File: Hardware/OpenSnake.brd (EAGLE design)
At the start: 25.4 x 69.8 mm, 53 parts, among them Q1 16MHZ, U1 ATMEGA328P_TQFP, U2 317

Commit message: Adjusted tValues for better assembly sheet, created assembly sheet PDF
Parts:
- U1: value ATMEGA328P_TQFP -> ATMEGA328P

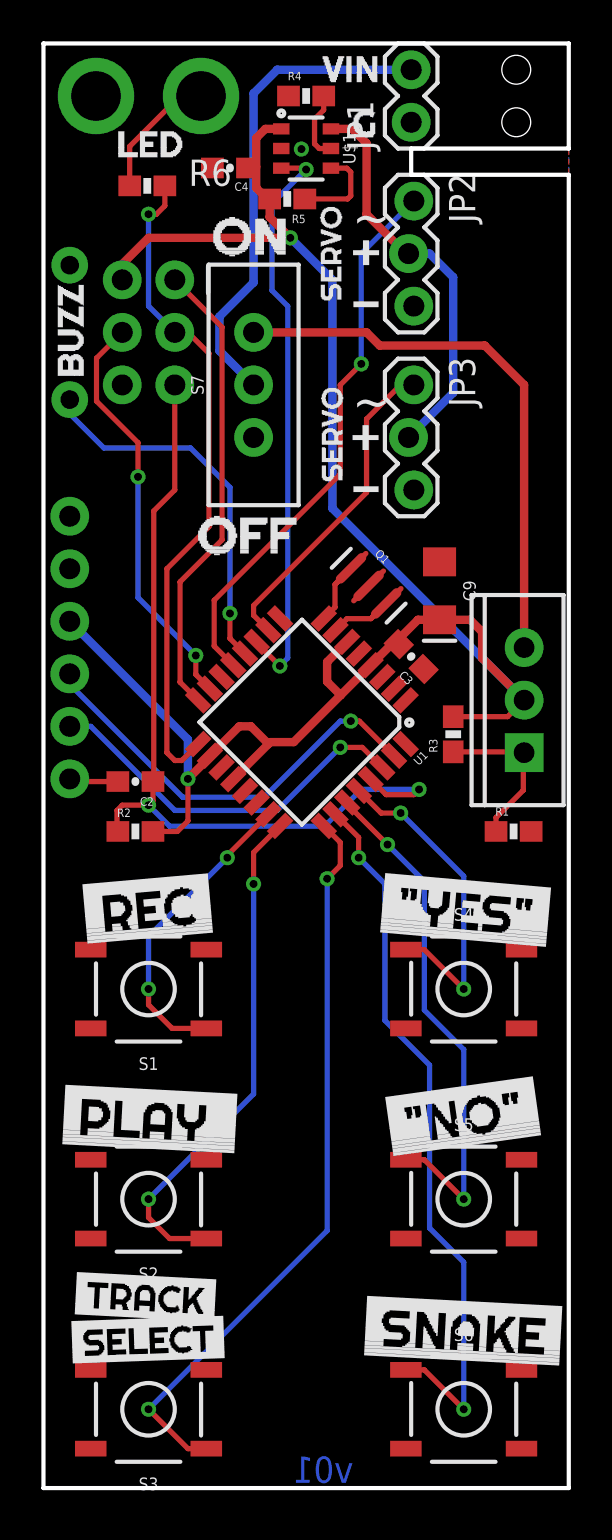
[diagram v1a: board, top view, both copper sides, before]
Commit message: Corrected RX/TX to 6-pin Serial programming header
I had these swapped on the header. Classic rookie mistake :)

-Swapped RX/TX on the serial header
-bumped version to v10 in sch and brd copper
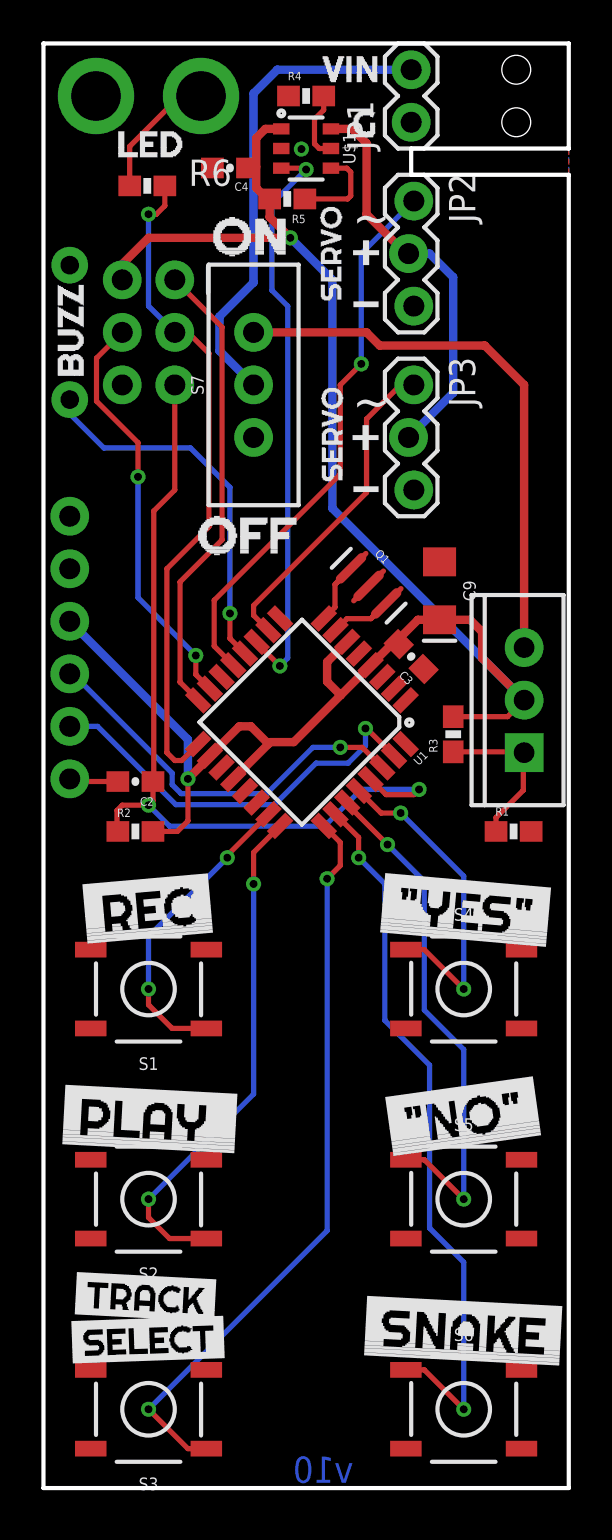
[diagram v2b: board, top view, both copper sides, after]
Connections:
- net RX: now also J1.P$3; no longer J1.P$2
- net TX: now also J1.P$2; no longer J1.P$3
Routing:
- net TX: track 20.7 -> 19.8 mm
- net RX: track 18.5 -> 19.2 mm
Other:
- board text added: "v10"
- board text removed: "v01"
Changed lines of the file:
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@@
 <wire x1="31.75" y1="52.07" x2="30.48" y2="53.34" width="0.2032" layer="49"/>
 <wire x1="31.75" y1="52.07" x2="30.48" y2="50.8" width="0.2032" layer="49"/>
-<text x="14.986" y="0.254" size="1.27" layer="16" font="vector" ratio="18" rot="MR0">v01</text>
+<text x="14.986" y="0.254" size="1.27" layer="16" font="vector" ratio="18" rot="MR0">v10</text>
 <rectangle x1="14.986" y1="57.0992" x2="16.2052" y2="57.3786" layer="21"/>
 <rectangle x1="14.986" y1="48.1584" x2="16.2052" y2="48.4378" layer="21"/>
@@
 <contactref element="U$1" pad="2"/>
 <contactref element="R4" pad="1"/>
-<contactref element="J1" pad="P$6"/>
-<contactref element="J1" pad="P$5"/>
 <polygon width="0.2032" layer="1">
 <vertex x="0" y="0"/>
@@
 <contactref element="LS1" pad="-"/>
 <via x="12.4714" y="64.7446" extent="1-16" drill="0.381"/>
+<contactref element="J1" pad="P$6"/>
+<contactref element="J1" pad="P$5"/>
 </signal>
 <signal name="SCK">
@@
 <wire x1="5.08" y1="57.15" x2="5.08" y2="61.595" width="0.254" layer="16"/>
 <via x="5.08" y="61.595" extent="1-16" drill="0.381"/>
-<wire x1="5.08" y1="61.595" x2="5.0520625" y2="61.6229375" width="0.254" layer="1"/>
 <wire x1="5.869040625" y1="62.003040625" x2="5.461" y2="61.595" width="0.254" layer="1"/>
 <wire x1="5.08" y1="61.595" x2="5.461" y2="61.595" width="0.254" layer="1"/>
@@
 <signal name="RX">
 <contactref element="U1" pad="30"/>
-<contactref element="J1" pad="P$2"/>
 <wire x1="16.382459375" y1="34.84459375" x2="15.413053125" y2="35.814" width="0.254" layer="1"/>
 <wire x1="15.413053125" y1="35.814" x2="14.351" y2="35.814" width="0.254" layer="1"/>
 <via x="14.351" y="35.814" extent="1-16" drill="0.381"/>
-<wire x1="14.351" y1="35.814" x2="11.303" y2="32.766" width="0.254" layer="16"/>
-<wire x1="2.286" y1="36.83" x2="1.27" y2="36.83" width="0.254" layer="16"/>
-<wire x1="11.303" y1="32.766" x2="6.35" y2="32.766" width="0.254" layer="16"/>
-<wire x1="6.35" y1="32.766" x2="2.286" y2="36.83" width="0.254" layer="16"/>
+<wire x1="14.351" y1="35.814" x2="13.0302" y2="35.814" width="0.254" layer="16"/>
+<wire x1="13.0302" y1="35.814" x2="10.795" y2="33.5788" width="0.254" layer="16"/>
+<wire x1="10.795" y1="33.5788" x2="6.6548" y2="33.5788" width="0.254" layer="16"/>
+<contactref element="J1" pad="P$3"/>
+<wire x1="6.223" y1="34.0106" x2="6.223" y2="34.5694" width="0.254" layer="16"/>
+<wire x1="6.223" y1="34.5694" x2="1.4224" y2="39.37" width="0.254" layer="16"/>
+<wire x1="1.4224" y1="39.37" x2="1.27" y2="39.37" width="0.254" layer="16"/>
+<wire x1="6.6548" y1="33.5788" x2="6.223" y2="34.0106" width="0.254" layer="16"/>
 </signal>
 <signal name="RST">
@@
 <signal name="TX">
 <contactref element="U1" pad="31"/>
-<contactref element="J1" pad="P$3"/>
-<wire x1="16.94814375" y1="35.410278125" x2="15.274421875" y2="37.084" width="0.254" layer="1"/>
-<wire x1="15.274421875" y1="37.084" x2="14.859" y2="37.084" width="0.254" layer="1"/>
-<via x="14.859" y="37.084" extent="1-16" drill="0.381"/>
-<wire x1="14.859" y1="37.084" x2="14.351" y2="37.084" width="0.254" layer="16"/>
-<wire x1="14.351" y1="37.084" x2="10.668" y2="33.401" width="0.254" layer="16"/>
-<wire x1="1.27" y1="38.862" x2="1.27" y2="39.37" width="0.254" layer="16"/>
-<wire x1="10.668" y1="33.401" x2="6.731" y2="33.401" width="0.254" layer="16"/>
-<wire x1="6.731" y1="33.401" x2="1.27" y2="38.862" width="0.254" layer="16"/>
+<wire x1="16.94814375" y1="35.410278125" x2="15.630021875" y2="36.7284" width="0.254" layer="1"/>
+<wire x1="15.630021875" y1="36.7284" x2="15.5702" y2="36.7284" width="0.254" layer="1"/>
+<via x="15.5702" y="36.7284" extent="1-16" drill="0.381"/>
+<contactref element="J1" pad="P$2"/>
+<wire x1="15.5702" y1="36.7284" x2="15.5702" y2="35.8902" width="0.254" layer="16"/>
+<wire x1="11.176" y1="33.0454" x2="6.4008" y2="33.0454" width="0.254" layer="16"/>
+<wire x1="2.6162" y1="36.83" x2="1.27" y2="36.83" width="0.254" layer="16"/>
+<wire x1="15.5702" y1="35.8902" x2="14.732" y2="35.052" width="0.254" layer="16"/>
+<wire x1="14.732" y1="35.052" x2="13.1826" y2="35.052" width="0.254" layer="16"/>
+<wire x1="13.1826" y1="35.052" x2="11.176" y2="33.0454" width="0.254" layer="16"/>
+<wire x1="6.4008" y1="33.0454" x2="2.6162" y2="36.83" width="0.254" layer="16"/>
 </signal>
 <signal name="SERVO_1">
